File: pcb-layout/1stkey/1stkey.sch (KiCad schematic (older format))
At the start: 13 parts

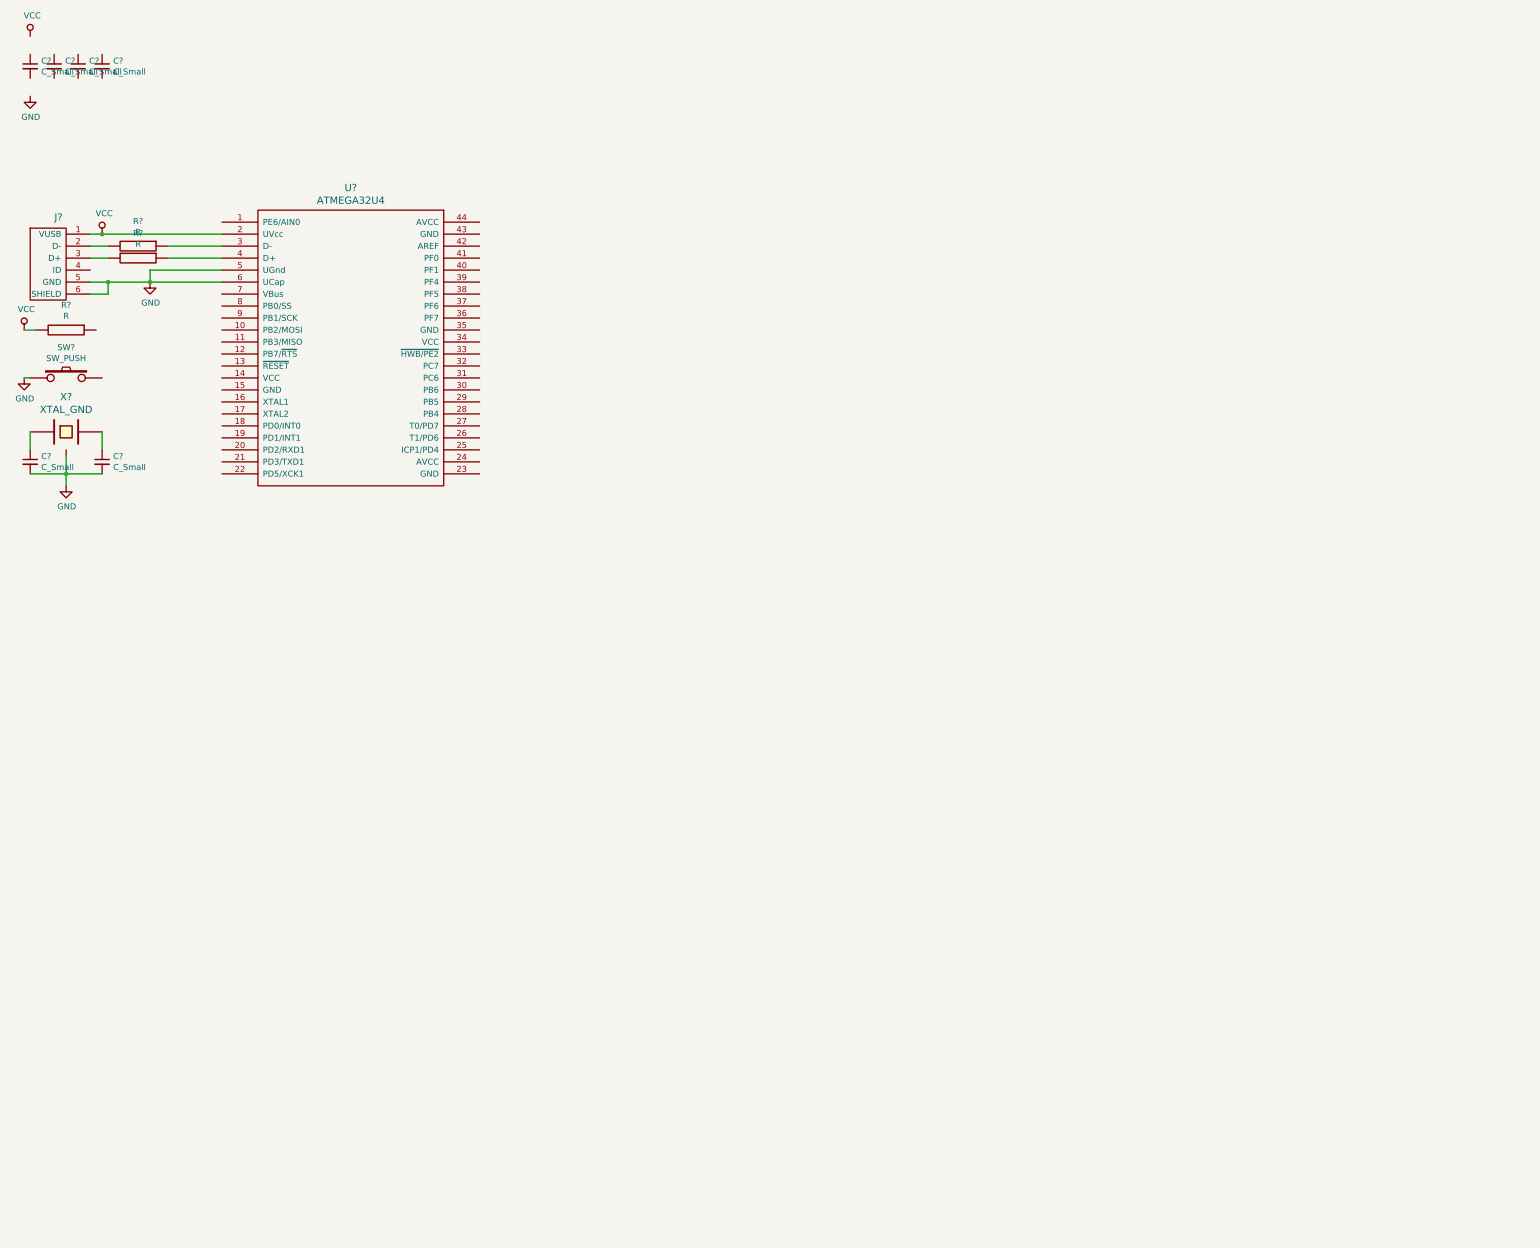
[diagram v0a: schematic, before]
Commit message: pcb começando a ser projetado
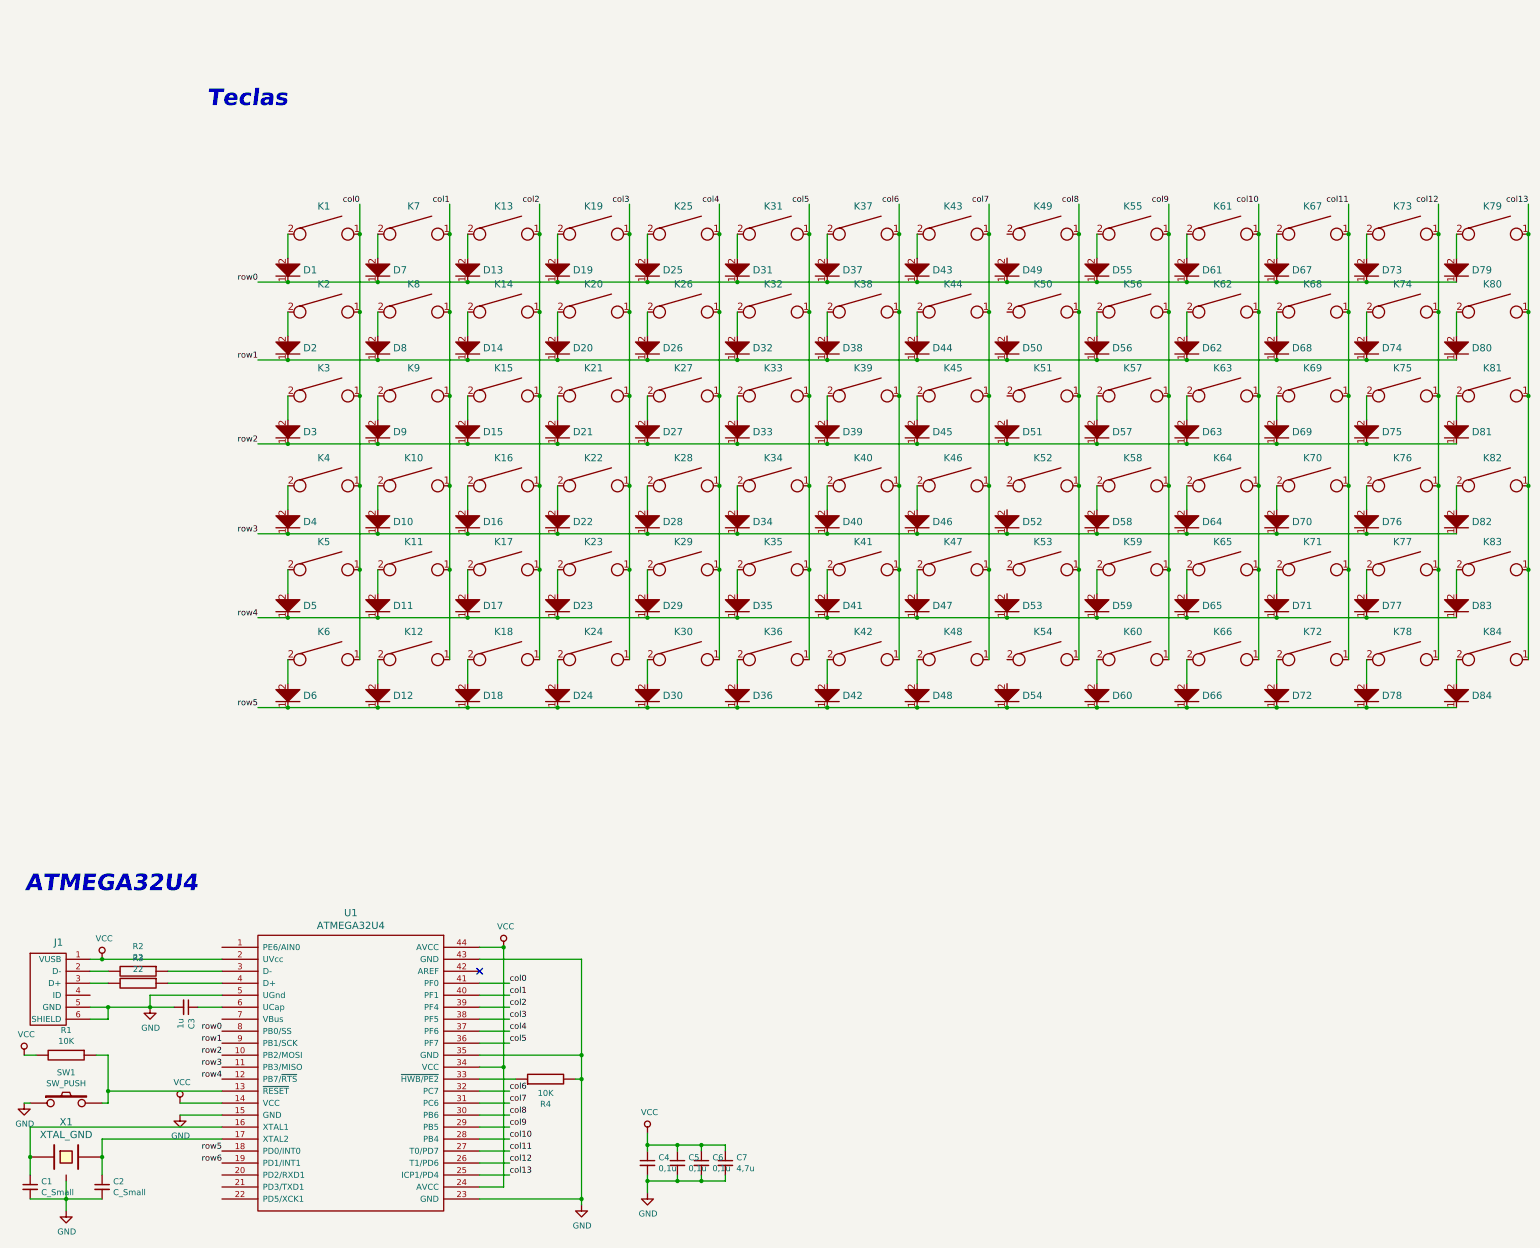
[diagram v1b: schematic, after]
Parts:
- removed C? (x3): C_Small, symbol Device:C_Small
- added C3: 1u, Capacitor_SMD:C_0805_2012Metric_Pad1.15x1.40mm_HandSolder, symbol Device:C_Small
- added C5, C6: 0,1u, Capacitor_SMD:C_0805_2012Metric_Pad1.15x1.40mm_HandSolder, symbol Device:C_Small
- added C7: 4,7u, Capacitor_SMD:C_0805_2012Metric_Pad1.15x1.40mm_HandSolder, symbol Device:C_Small
- added D1, D10, D11, D12, D13, D14, D15, D16, D17, D18, D19, D2, D20, D21, D22, D23, D24, D25, D26, D27, D28, D29, D3, D30, D31, D32, D33, D34, D35, D36, D37, D38, D39, D4, D40, D41, D42, D43, D44, D45, D46, D47, D48, D49, D5, D50, D51, D52, D53, D54, D55, D56, D57, D58, D59, D6, D60, D61, D62, D63, D64, D65, D66, D67, D68, D69, D7, D70, D71, D72, D73, D74, D75, D76, D77, D78, D79, D8, D80, D81, D82, D83, D84, D9: D, keyboard_parts:D_SOD123_axial, symbol keyboard_parts:D
- added K1, K10, K11, K12, K13, K14, K15, K16, K17, K18, K19, K2, K20, K21, K22, K23, K24, K25, K26, K27, K28, K29, K3, K30, K31, K32, K33, K34, K35, K36, K37, K38, K39, K4, K40, K41, K42, K43, K44, K45, K46, K47, K48, K49, K5, K50, K51, K52, K53, K54, K55, K56, K57, K58, K59, K6, K60, K61, K62, K63, K64, K65, K66, K67, K68, K69, K7, K70, K71, K72, K73, K74, K75, K76, K77, K78, K79, K8, K80, K81, K82, K83, K84, K9: KEYSW, keebs:Mx_Alps_100, symbol keyboard_parts:KEYSW
- added R4: 10K, Resistor_SMD:R_0805_2012Metric_Pad1.15x1.40mm_HandSolder, symbol keyboard_parts:R
- C1, C2: renamed from C?; footprint (none) -> Capacitor_SMD:C_0805_2012Metric_Pad1.15x1.40mm_HandSolder
- C4: renamed from C?; value C_Small -> 0,1u; footprint (none) -> Capacitor_SMD:C_0805_2012Metric_Pad1.15x1.40mm_HandSolder
- J1: renamed from J?; footprint (none) -> keyboard_parts:USB_miniB_hirose_5S8
- R1: renamed from R?; value R -> 10K; footprint (none) -> Resistor_SMD:R_0805_2012Metric_Pad1.15x1.40mm_HandSolder
- R2, R3: renamed from R?; value R -> 22; footprint (none) -> Resistor_SMD:R_0805_2012Metric_Pad1.15x1.40mm_HandSolder
- SW1: renamed from SW?; footprint (none) -> Button_Switch_SMD:SW_SPST_TL3342
- U1: renamed from U?; footprint (none) -> Package_QFP:TQFP-44_10x10mm_P0.8mm
- X1: renamed from X?; footprint (none) -> Crystal:Crystal_SMD_SeikoEpson_TSX3225-4Pin_3.2x2.5mm_HandSoldering
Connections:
- net GND: now also C4.2, U1.15 (GND), U1.23 (GND), U1.35 (GND), U1.43 (GND), C3.2, C5.2, C6.2, C7.2, R4.2; no longer U1.6 (UCap)
- net VCC: now also C4.1, U1.14 (VCC), U1.24 (AVCC), U1.34 (VCC), U1.44 (AVCC), C5.1, C6.1, C7.1
- net row2: now reaches U1.10 (PB2/MOSI)
- net row2: now also D15.1, D21.1, D27.1, D3.1, D33.1, D39.1, D45.1, D51.1, D57.1, D63.1, D69.1, D75.1, D81.1, D9.1
- net row3: now reaches U1.11 (PB3/MISO)
- net row3: now also D10.1, D16.1, D22.1, D28.1, D34.1, D4.1, D40.1, D46.1, D52.1, D58.1, D64.1, D70.1, D76.1, D82.1
- net row4: now reaches U1.12 (PB7/~RTS)
- net row4: now also D11.1, D17.1, D23.1, D29.1, D35.1, D41.1, D47.1, D5.1, D53.1, D59.1, D65.1, D71.1, D77.1, D83.1
- net at U1.13 (~RESET): now also R1.1, SW1.2
- net at U1.16 (XTAL1): now also C1.1, X1.1
- net at U1.17 (XTAL2): now also C2.1, X1.2
- net row5: now reaches U1.18 (PD0/INT0)
- net row5: now also D12.1, D18.1, D24.1, D30.1, D36.1, D42.1, D48.1, D54.1, D6.1, D60.1, D66.1, D72.1, D78.1, D84.1
- net row6: now reaches U1.19 (PD1/INT1)
- net col13: now reaches U1.25 (ICP1/PD4)
- net col13: now also K79.1, K80.1, K81.1, K82.1, K83.1, K84.1
- net col12: now reaches U1.26 (T1/PD6)
- net col12: now also K73.1, K74.1, K75.1, K76.1, K77.1, K78.1
- net col11: now reaches U1.27 (T0/PD7)
- net col11: now also K67.1, K68.1, K69.1, K70.1, K71.1, K72.1
- net col10: now reaches U1.28 (PB4)
- net col10: now also K61.1, K62.1, K63.1, K64.1, K65.1, K66.1
- net col9: now reaches U1.29 (PB5)
- net col9: now also K55.1, K56.1, K57.1, K58.1, K59.1, K60.1
- net col8: now reaches U1.30 (PB6)
- net col8: now also K49.1, K50.1, K51.1, K52.1, K53.1, K54.1
- net col7: now reaches U1.31 (PC6)
- net col7: now also K43.1, K44.1, K45.1, K46.1, K47.1, K48.1
- net col6: now reaches U1.32 (PC7)
- net col6: now also K37.1, K38.1, K39.1, K40.1, K41.1, K42.1
- net at U1.33 (~HWB/PE2): now also R4.1
- net col5: now reaches U1.36 (PF7)
- net col5: now also K31.1, K32.1, K33.1, K34.1, K35.1, K36.1
- net col4: now reaches U1.37 (PF6)
- net col4: now also K25.1, K26.1, K27.1, K28.1, K29.1, K30.1
- net col3: now reaches U1.38 (PF5)
- net col3: now also K19.1, K20.1, K21.1, K22.1, K23.1, K24.1
- net col2: now reaches U1.39 (PF4)
- net col2: now also K13.1, K14.1, K15.1, K16.1, K17.1, K18.1
- net col1: now reaches U1.40 (PF1)
- net col1: now also K10.1, K11.1, K12.1, K7.1, K8.1, K9.1
- net col0: now reaches U1.41 (PF0)
- net col0: now also K1.1, K2.1, K3.1, K4.1, K5.1, K6.1
- net row0: now reaches U1.8 (PB0/SS)
- net row0: now also D1.1, D13.1, D19.1, D25.1, D31.1, D37.1, D43.1, D49.1, D55.1, D61.1, D67.1, D7.1, D73.1, D79.1
- net row1: now reaches U1.9 (PB1/SCK)
- net row1: now also D14.1, D2.1, D20.1, D26.1, D32.1, D38.1, D44.1, D50.1, D56.1, D62.1, D68.1, D74.1, D8.1, D80.1
- new net: C3.1, U1.6 (UCap)
- new net: D1.2, K1.2
- new net: D7.2, K7.2
- new net: D2.2, K2.2
- new net: D8.2, K8.2
- new net: D13.2, K13.2
- new net: D19.2, K19.2
- new net: D25.2, K25.2
- new net: D31.2, K31.2
- new net: D37.2, K37.2
- new net: D43.2, K43.2
- new net: D55.2, K55.2
- new net: D61.2, K61.2
- new net: D67.2, K67.2
- new net: D73.2, K73.2
- new net: D79.2, K79.2
- new net: D14.2, K14.2
- new net: D20.2, K20.2
- new net: D26.2, K26.2
- new net: D32.2, K32.2
- new net: D38.2, K38.2
- new net: D44.2, K44.2
- new net: D56.2, K56.2
- new net: D62.2, K62.2
- new net: D68.2, K68.2
- new net: D74.2, K74.2
- new net: D80.2, K80.2
- new net: D15.2, K15.2
- new net: D21.2, K21.2
- new net: D27.2, K27.2
- new net: D33.2, K33.2
- new net: D39.2, K39.2
- new net: D45.2, K45.2
- new net: D57.2, K57.2
- new net: D63.2, K63.2
- new net: D69.2, K69.2
- new net: D75.2, K75.2
- new net: D81.2, K81.2
- new net: D3.2, K3.2
- new net: D9.2, K9.2
- new net: D16.2, K16.2
- new net: D22.2, K22.2
- new net: D28.2, K28.2
- new net: D34.2, K34.2
- new net: D40.2, K40.2
- new net: D46.2, K46.2
- new net: D58.2, K58.2
- new net: D64.2, K64.2
- new net: D70.2, K70.2
- new net: D76.2, K76.2
- new net: D82.2, K82.2
- new net: D4.2, K4.2
- new net: D10.2, K10.2
- new net: D17.2, K17.2
- new net: D23.2, K23.2
- new net: D29.2, K29.2
- new net: D35.2, K35.2
- new net: D41.2, K41.2
- new net: D47.2, K47.2
- new net: D59.2, K59.2
- new net: D65.2, K65.2
- new net: D71.2, K71.2
- new net: D77.2, K77.2
- new net: D83.2, K83.2
- new net: D5.2, K5.2
- new net: D11.2, K11.2
- new net: D18.2, K18.2
- new net: D24.2, K24.2
- new net: D30.2, K30.2
- new net: D36.2, K36.2
- new net: D42.2, K42.2
- new net: D48.2, K48.2
- new net: D60.2, K60.2
- new net: D66.2, K66.2
- new net: D72.2, K72.2
- new net: D78.2, K78.2
- new net: D84.2, K84.2
- new net: D6.2, K6.2
- new net: D12.2, K12.2
- no-connect marks 0 -> 1
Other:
- note added: "ATMEGA32U4"
- note added: "Teclas\n"
- moved on the sheet: C1, C2, C4, J1, R1, R2, R3, SW1, U1, X1
